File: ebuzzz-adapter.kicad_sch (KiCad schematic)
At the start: 39 parts, among them J1 USB_A, J4 EBUS, Q1 BC817-40, U1 LTV-357T, U2 LTV-357T, U3 LM2903DT, U4 LP2951-50DR, U5 CP2104

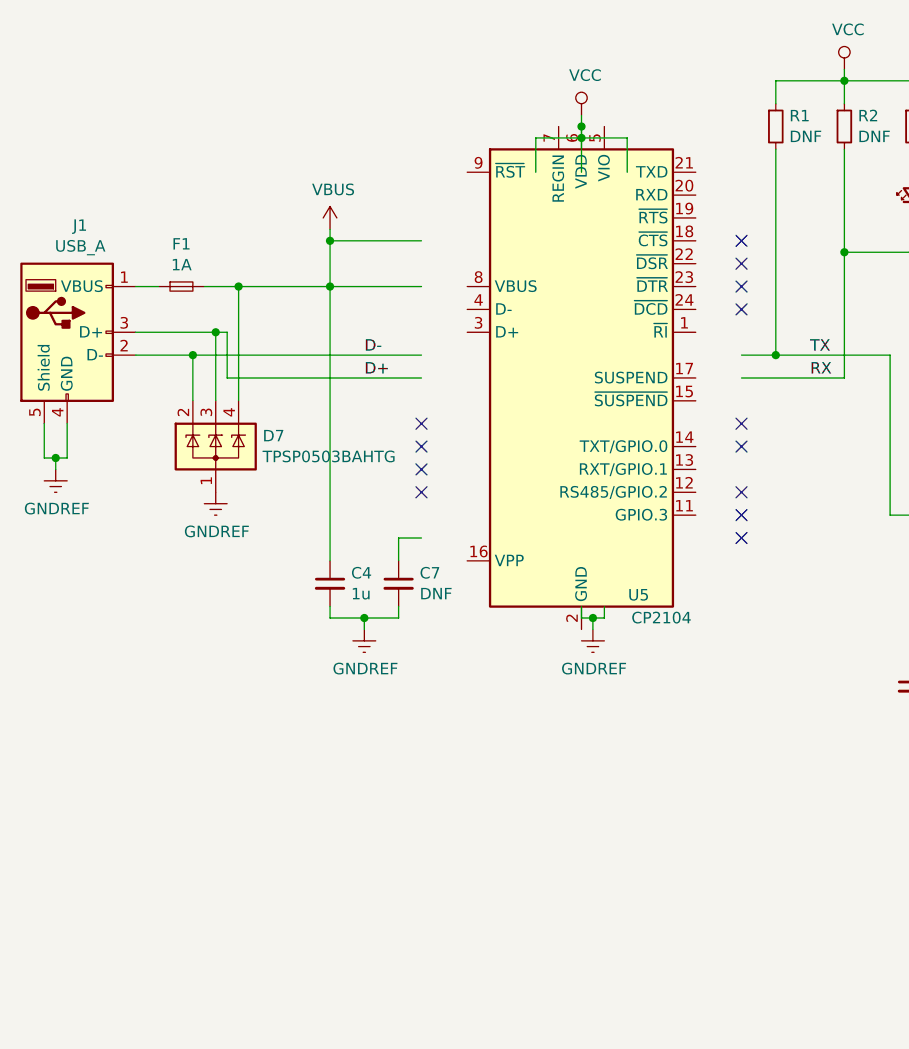
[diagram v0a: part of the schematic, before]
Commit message: Fixed schematics after KiCad 6.0 upgrade.
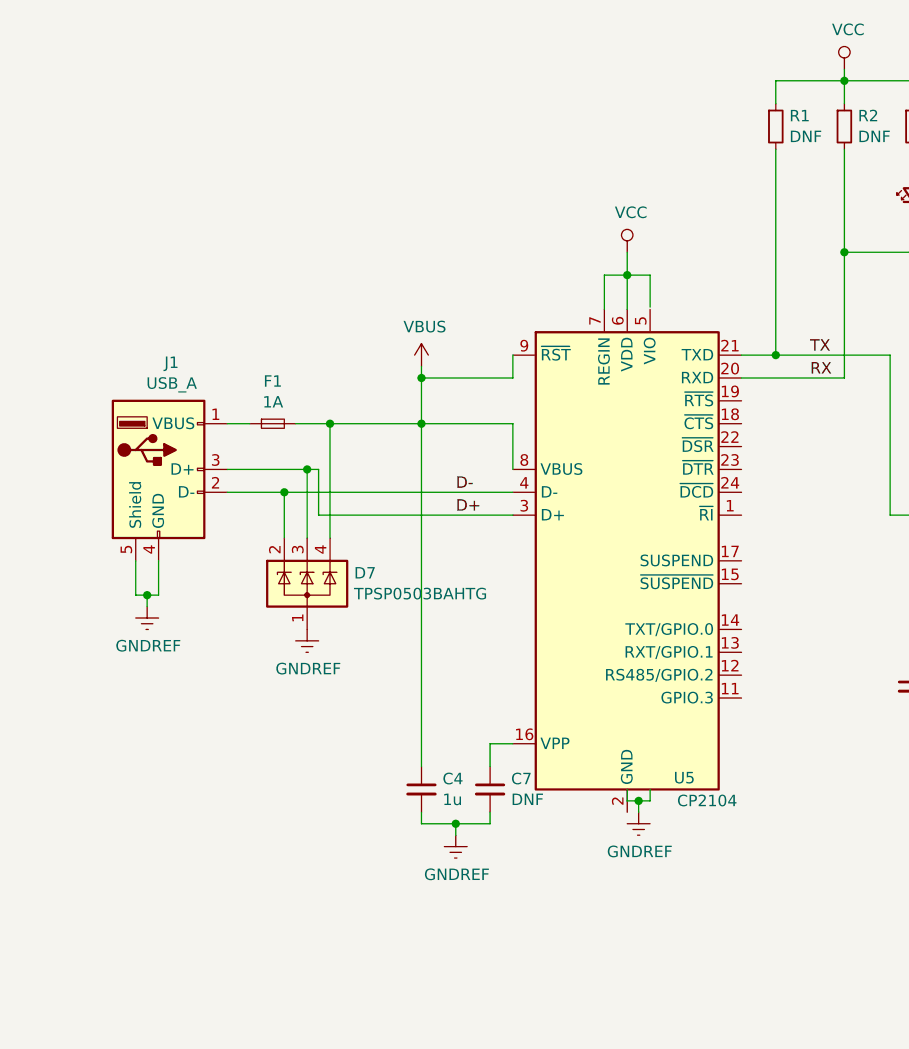
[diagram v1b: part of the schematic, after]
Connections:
- net D+: now also U5.3 (D+)
- net D-: now also U5.4 (D-)
- net RX: now also U5.20 (RXD)
- net TX: now also U5.21 (TXD)
- net VBUS: now also U5.8 (VBUS), U5.9 (~{RST})
- net VCC: now also U5.7 (REGIN)
- net at U5.16 (VPP): now also C7.1
- no-connect marks 14 -> 1
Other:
- moved on the sheet: C4, C7, D7, F1, J1, U5
